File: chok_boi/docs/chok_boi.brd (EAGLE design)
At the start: 160 x 100 mm, 94 parts, among them IC1 L293DD, U1 MPU-6000

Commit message: Place all big components on board
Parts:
- removed U$10: EMITTER, sfh4550 _ teft4300:EMITTER
- removed U$6: RECEIVER, sfh4550 _ teft4300:RECEIVER
- added LEFT_FRONT_EMITTER: EMITTER, sfh4550 _ teft4300:EMITTER
- added REC_LF: RECEIVER, sfh4550 _ teft4300:RECEIVER
- moved T1 370.0 mm to (16.0, 13.5)
- moved T3 352.3 mm to (17.0, 59.2)
- moved L1 350.4 mm to (16.3, 19.8)
- moved B1 349.5 mm to (5.59, 4.06)
- moved U$20 348.2 mm to (65.8, 10.4), turned to 180 degrees
- moved T2 344.8 mm to (13.5, 59.7)
- moved SERIAL2 344.5 mm to (56.9, 52.3)
- moved U1 343.9 mm to (69.1, 36.8)
- moved C_BAT2 342.3 mm to (13.2, 48.3)
- moved C_5V2 340.4 mm to (13.2, 44.7)
- moved B0 339.5 mm to (5.59, 10.7)
- moved U$8 336.4 mm to (73.9, 20.1), turned to 218.7 degrees
- moved U$9 336.3 mm to (77.5, 32.8), turned to 270 degrees
- moved SERIAL1 332.1 mm to (56.6, 57.4)
- moved LED_PWR 332.0 mm to (13.2, 51.8)
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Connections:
- net N$14 renamed H_EM
- net N$15 renamed H2_EM
- net N$17 renamed D2_EM
- net N$27 renamed RF_EM
- net N$9 renamed D_EM
- removed net N$5: R_ELF.2, U$10.-
- new net LF_EM: LEFT_FRONT_EMITTER.-, R_ELF.2
- net 5V: now also LEFT_FRONT_EMITTER.+; no longer U$10.+
- net A3.3V: now also REC_LF.C; no longer U$6.C
- net REC_LF: now also REC_LF.E; no longer U$6.E

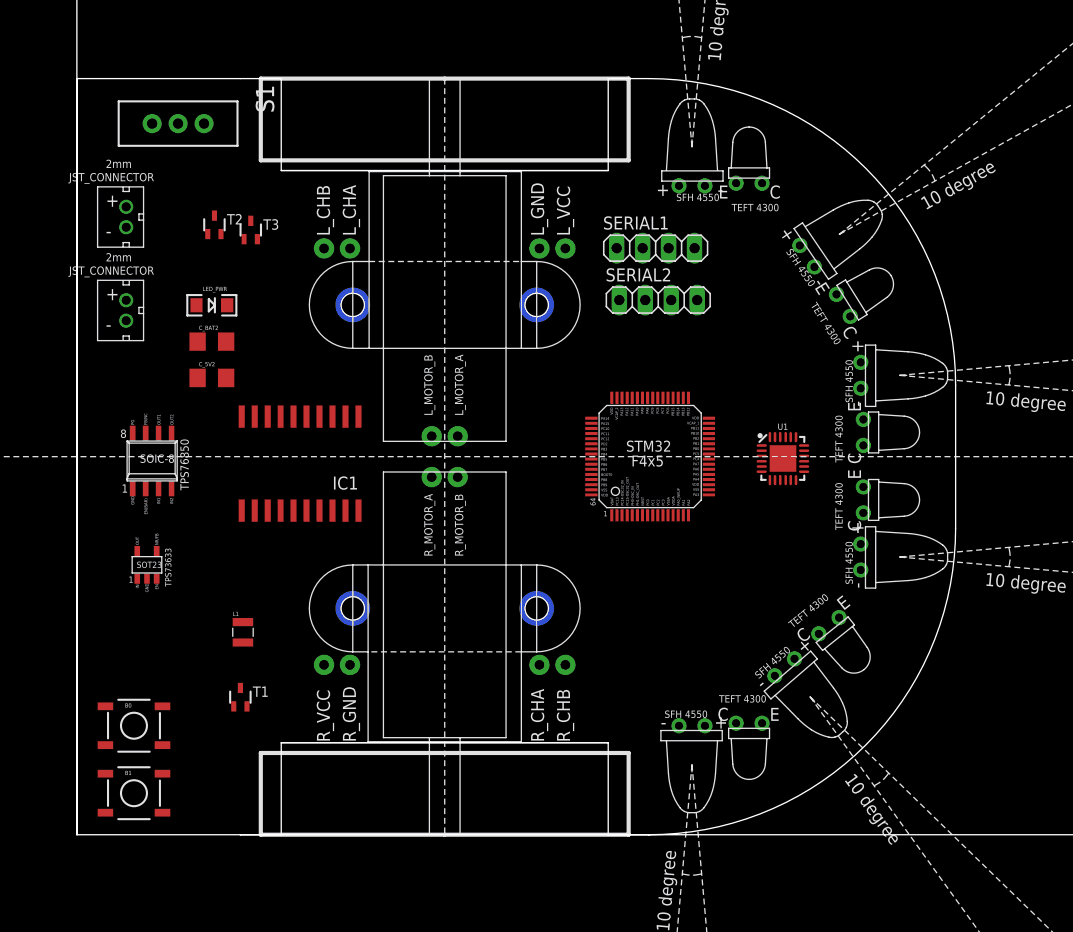
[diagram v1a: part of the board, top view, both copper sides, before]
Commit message: Add power and gnd planes
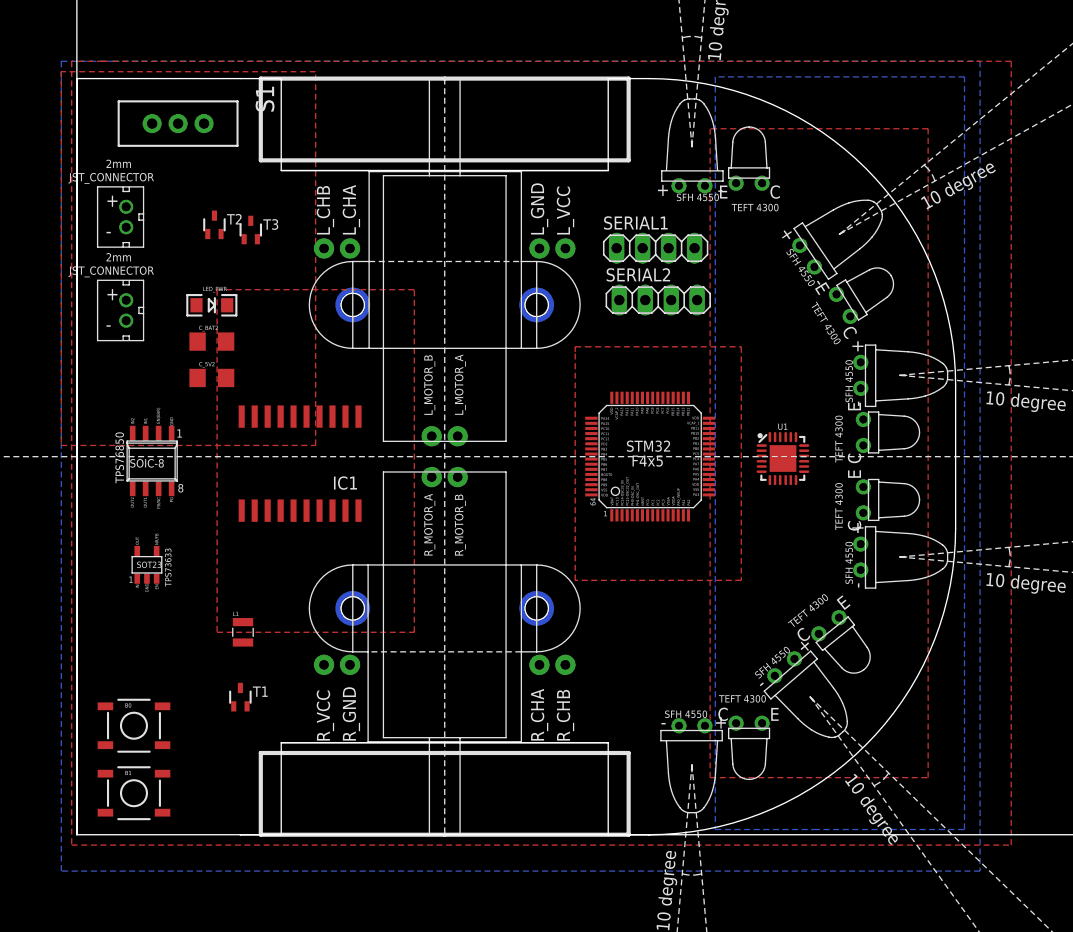
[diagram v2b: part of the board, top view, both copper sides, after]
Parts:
- turned U$4 to 180 degrees
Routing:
- added copper zone on layer 1, net 3.3V
- added copper zone on layer 1, net 5V
- added copper zone on layer 1, net A3.3V
- added copper zone on layer 16, net AGND
- added copper zone on layer 1, net BATTERY
- added copper zone on layer 16, net GND
- added copper zone on layer 1, net MGND

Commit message: Change part names for easier routing
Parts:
- removed C_5V4, C_5V5, C_5V6, C_5V7, C_5V8, C_5V9: 0.1uF, SparkFun:0603-CAP
- removed C_ERF3, C_S2: 0.1uF, SparkFun-Capacitors:0603-CAP
- removed C_ERF4, C_S1: 4.7uF, SparkFun-Capacitors:0603-CAP
- removed R_ES1, R_ES2, R_ES3, R_ES4: 5.6, SparkFun-Passives:0603-RES
- removed R_RLS, R_RRF1, R_RRF2, R_RRS: 1.8k, SparkFun-Passives:0603-RES
- added C_EM_D1, C_E_H1: 4.7uF, SparkFun-Capacitors:0603-CAP
- added C_EM_D2, C_E_H2: 0.1uF, SparkFun-Capacitors:0603-CAP
- added C_REC_LD, C_REC_LF, C_REC_LH, C_REC_RD, C_REC_RF, C_REC_RH: 0.1uF, SparkFun:0603-CAP
- added R_ED1, R_ED2, R_EH1, R_EH2: 5.6, SparkFun-Passives:0603-RES
- added R_RLD, R_RLH, R_RRD, R_RRH: 1.8k, SparkFun-Passives:0603-RES
- moved R_RRF 436.6 mm to (73.7, 25.7)
- moved R_RLF 417.1 mm to (73.2, 44.5)
- moved U$16 408.5 mm to (20.6, 44.5)
- moved U$15 405.7 mm to (20.6, 46.0)
- moved C_3.3V1 356.8 mm to (196.6, 92.7)
- moved C_3.3V2 356.8 mm to (192.8, 92.7)
- moved C_5V1 356.8 mm to (189.0, 92.7)
- moved C_5V10 356.8 mm to (162.3, 92.7)
- moved C_5V11 356.8 mm to (158.5, 92.7)
- moved C_5V12 356.8 mm to (154.7, 92.7)
- moved C_BAT1 356.8 mm to (150.9, 92.7)
- moved C_ELF1 356.8 mm to (147.1, 92.7)
- moved C_ELF2 356.8 mm to (143.3, 92.7)
- moved C_ERF1 356.8 mm to (139.4, 92.7)
- moved C_ERF2 356.8 mm to (135.6, 92.7)
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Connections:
- net 5V: now also C_EM_D1.1, C_EM_D2.1, C_E_H1.1, C_E_H2.1; no longer C_ERF3.1, C_ERF4.1, C_S1.1, C_S2.1
- net A3.3V: now also C_REC_LD.1, C_REC_LF.1, C_REC_LH.1, C_REC_RD.1, C_REC_RF.1, C_REC_RH.1; no longer C_5V4.1, C_5V5.1, C_5V6.1, C_5V7.1, C_5V8.1, C_5V9.1
- net AGND: now also C_REC_LD.2, C_REC_LF.2, C_REC_LH.2, C_REC_RD.2, C_REC_RF.2, C_REC_RH.2, R_RLD.1, R_RLH.1, R_RRD.1, R_RRH.1; no longer C_5V4.2, C_5V5.2, C_5V6.2, C_5V7.2, C_5V8.2, C_5V9.2, R_RLS.1, R_RRF1.1, R_RRF2.1, R_RRS.1
- net D2_EM: now also R_ED1.2, R_ED2.2; no longer R_ES1.2, R_ES2.2
- net GND: now also C_EM_D1.2, C_EM_D2.2, C_E_H1.2, C_E_H2.2; no longer C_ERF3.2, C_ERF4.2, C_S1.2, C_S2.2
- net H2_EM: now also R_EH1.2, R_EH2.2; no longer R_ES3.2, R_ES4.2
- net N$18: now also R_ED1.1, R_ED2.1; no longer R_ES1.1, R_ES2.1
- net N$19: now also R_EH1.1, R_EH2.1; no longer R_ES3.1, R_ES4.1
- net REC_LD: now also R_RLD.2; no longer R_RLS.2
- net REC_LH: now also R_RLH.2; no longer R_RRF2.2
- net REC_RD: now also R_RRD.2; no longer R_RRS.2
- net REC_RH: now also R_RRH.2; no longer R_RRF1.2

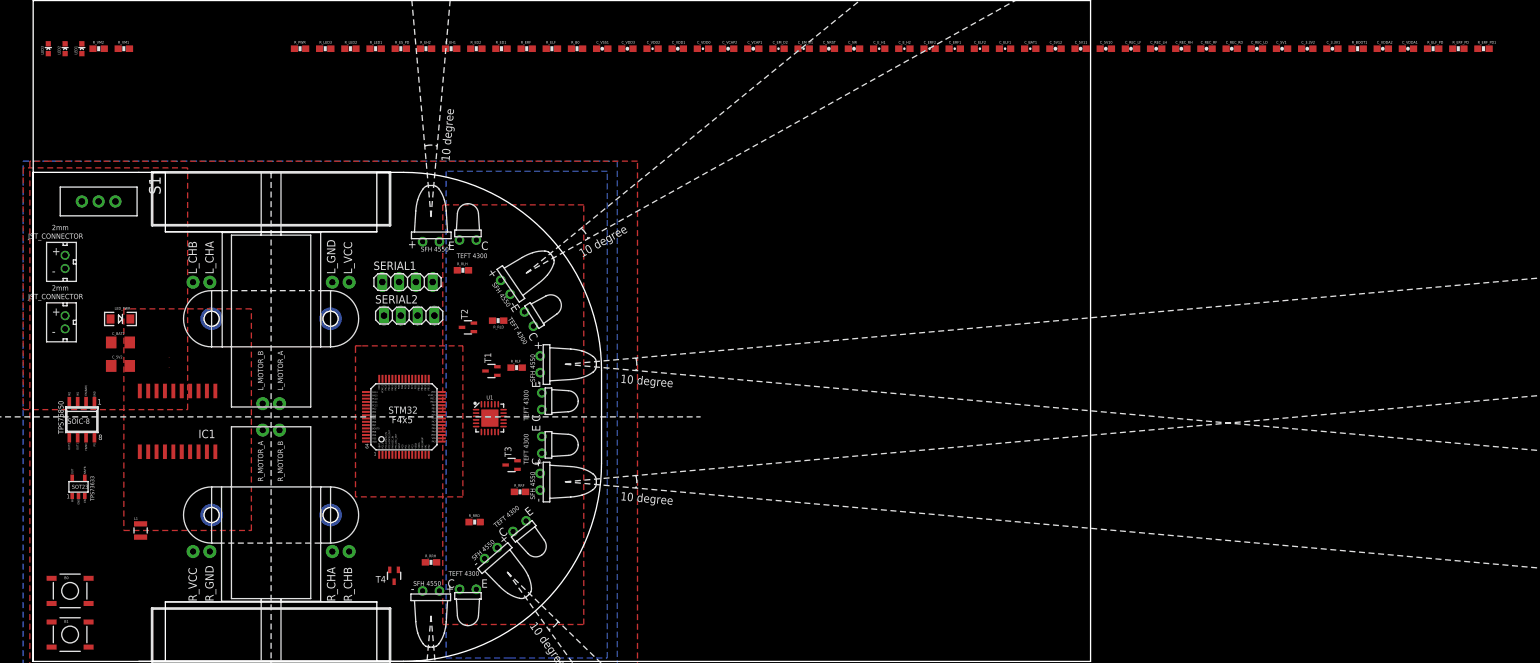
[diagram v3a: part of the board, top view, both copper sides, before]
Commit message: Finish component placement. Start routing
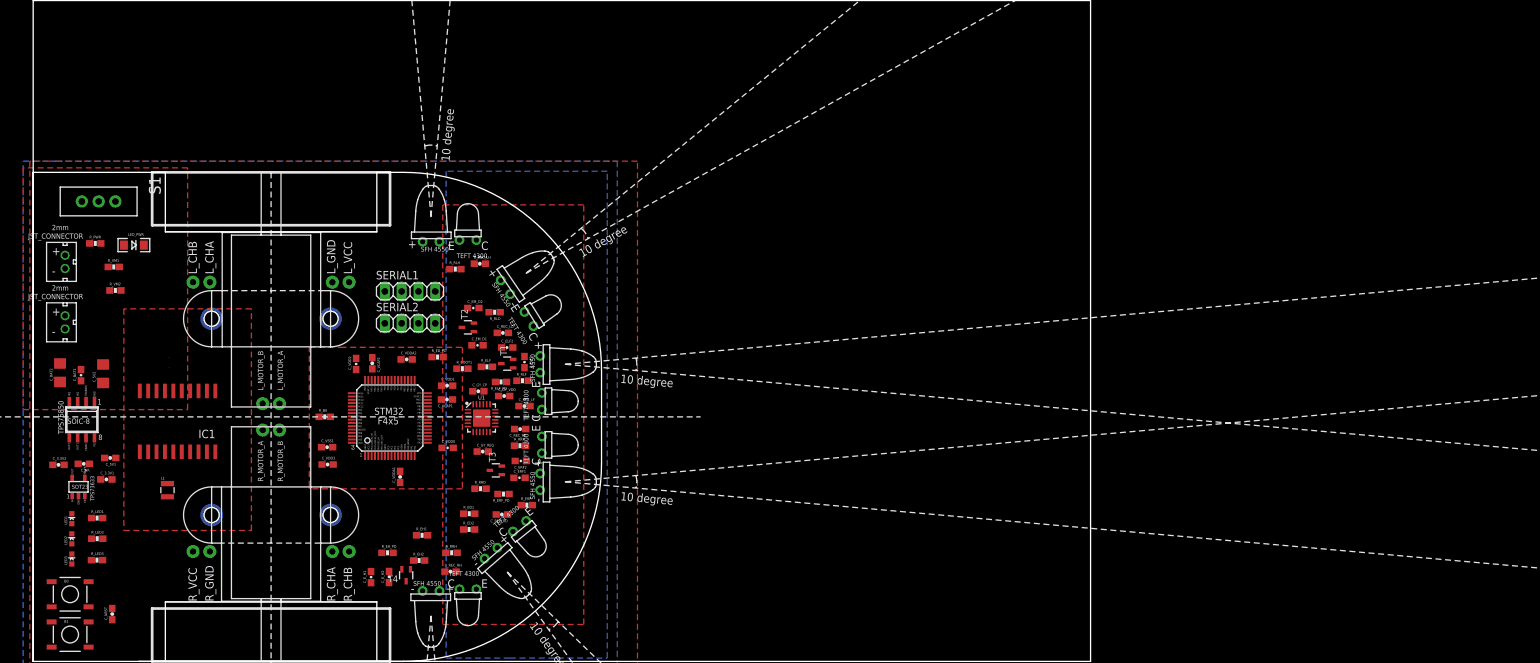
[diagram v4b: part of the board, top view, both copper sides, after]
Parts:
- removed C_5V10: 0.01uF, SparkFun:0603-CAP
- removed C_5V11: 0.1uF, SparkFun:0603-CAP
- removed C_5V12: 2.2nF, SparkFun:0603-CAP
- removed R_ERF_PD1, R_ES_PD: 47k, SparkFun-Passives:0603-RES
- added C_GY_CP: 2.2nF, SparkFun:0603-CAP
- added C_GY_REG: 0.1uF, SparkFun:0603-CAP
- added C_GY_VDD: 0.01uF, SparkFun:0603-CAP
- added R_ED_PD, R_EH_PD: 47k, SparkFun-Passives:0603-RES
- moved C_3.3V2 199.2 mm to (3.84, 29.7)
- moved C_3.3V1 196.6 mm to (11.1, 27.5)
- moved C_5V1 187.8 mm to (11.7, 30.8), turned to 180 degrees
- moved C_VDDA1 165.7 mm to (55.5, 27.9), turned to 90 degrees
- moved R_ERF_PD 159.4 mm to (71.2, 25.3), turned to 180 degrees
- moved C_VDDA2 155.0 mm to (56.5, 45.7)
- moved C_BAT1 151.9 mm to (7.24, 43.3), turned to 90 degrees
- moved R_ELF_PD 149.8 mm to (70.8, 42.3), turned to 180 degrees
- moved R_BOOT1 143.8 mm to (64.9, 44.3)
- moved C_NRST 138.1 mm to (12.0, 7.16), turned to 90 degrees
- moved C_REC_RH 136.0 mm to (63.1, 13.6)
- moved C_NR 132.4 mm to (7.65, 29.9), turned to 180 degrees
- moved C_REC_RD 131.0 mm to (70.9, 22.2), turned to 180 degrees
- moved C_REC_LD 121.9 mm to (71.1, 49.7)
- moved C_REC_RF 118.7 mm to (73.7, 35.2), turned to 180 degrees
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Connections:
- net A3.3V: now also C_GY_VDD.1; no longer C_5V10.1
- net AGND: now also C_GY_CP.2, C_GY_REG.2, C_GY_VDD.2; no longer C_5V10.2, C_5V11.2, C_5V12.2
- net EM_D: now also R_ED_PD.2; no longer R_ES_PD.2
- net EM_H: now also R_EH_PD.2; no longer R_ERF_PD1.2
- net GND: now also R_ED_PD.1, R_EH_PD.1; no longer R_ERF_PD1.1, R_ES_PD.1
- net N$20: now also C_GY_REG.1; no longer C_5V11.1
- net N$22: now also C_GY_CP.1; no longer C_5V12.1

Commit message: 117 Airwires Left
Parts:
- moved C_VDDA2 17.6 mm to (57.5, 28.2), turned to 270 degrees
- moved L1 9.15 mm to (11.3, 24.5), turned to 90 degrees
- moved R_VM1 5.97 mm to (16.3, 55.3)
- moved R_VM2 3.09 mm to (14.3, 58.6)
- moved C_VDD3 1.15 mm to (44.5, 30.9)
- moved R_LED3 1.13 mm to (9.07, 16.3), turned to 180 degrees
- moved C_VSS1 0.94 mm to (44.6, 33.4)
- moved R_LED1 0.77 mm to (8.92, 21.6), turned to 180 degrees
- moved R_LED2 0.76 mm to (9.03, 18.9), turned to 180 degrees
- moved C_VDDA1 0.60 mm to (55.0, 28.2)
- moved C_ERF1 0.31 mm to (73.8, 28.0), turned to 180 degrees
- moved B0 0.14 mm to (5.64, 10.0)
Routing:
- net GND: track 0.00 -> 203.2 mm, vias 0 -> 3
- net 5V: track 0.00 -> 87.1 mm, vias 0 -> 4
- net BATTERY: track 0.00 -> 26.2 mm, vias 0 -> 2
- net 3.3V: track 0.00 -> 23.9 mm
- net AGND: track 0.00 -> 11.1 mm
- net N$8: track 0.00 -> 10.7 mm
- net H2_EM: track 0.00 -> 9.44 mm
- net N$2: track 0.00 -> 9.20 mm
- net N$19: track 0.00 -> 8.82 mm
- net D2_EM: track 0.00 -> 7.43 mm
- net N$1: track 0.00 -> 7.14 mm
- net REC_RH: track 0.00 -> 6.92 mm
- net A3.3V: track 0.00 -> 5.77 mm
- net VOLTMETER: track 0.00 -> 4.40 mm
- net BOOT0: track 0.00 -> 4.40 mm
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- removed copper zone on layer 1, net A3.3V

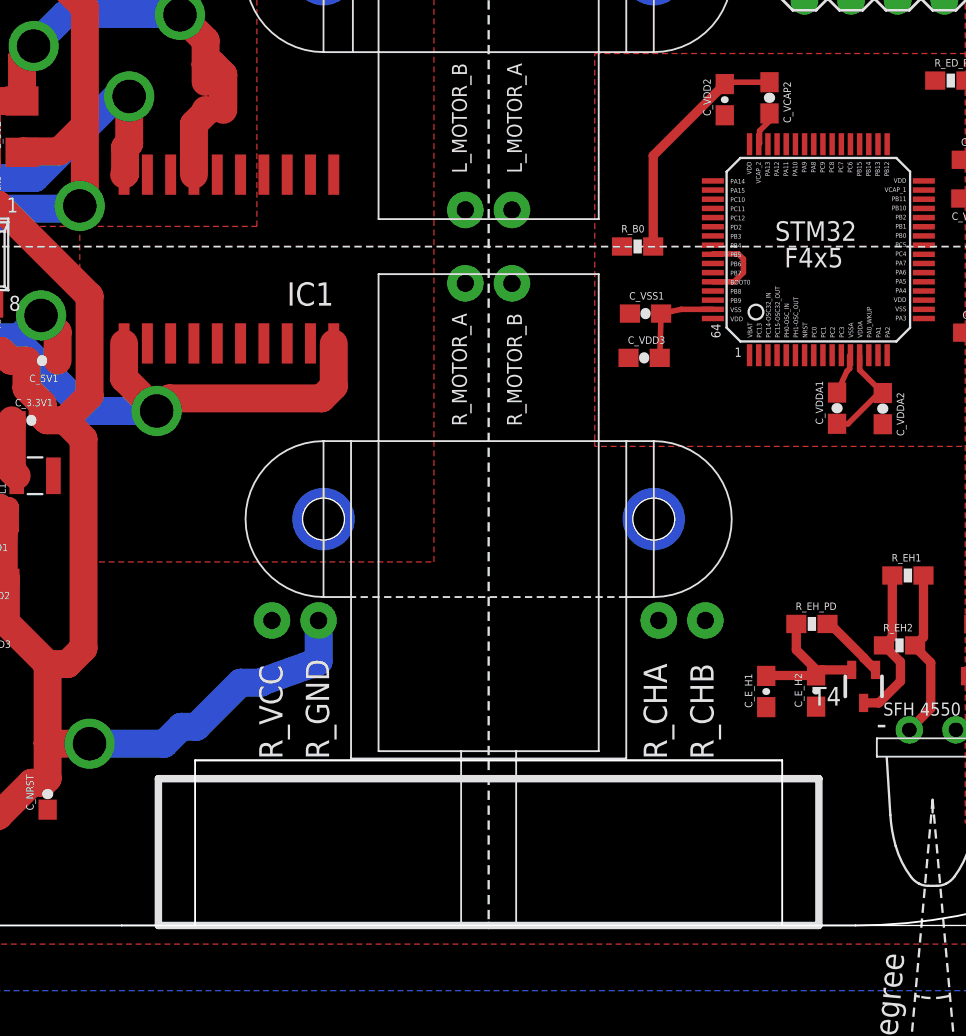
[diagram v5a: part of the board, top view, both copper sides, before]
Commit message: Add DRV8835 motor driver
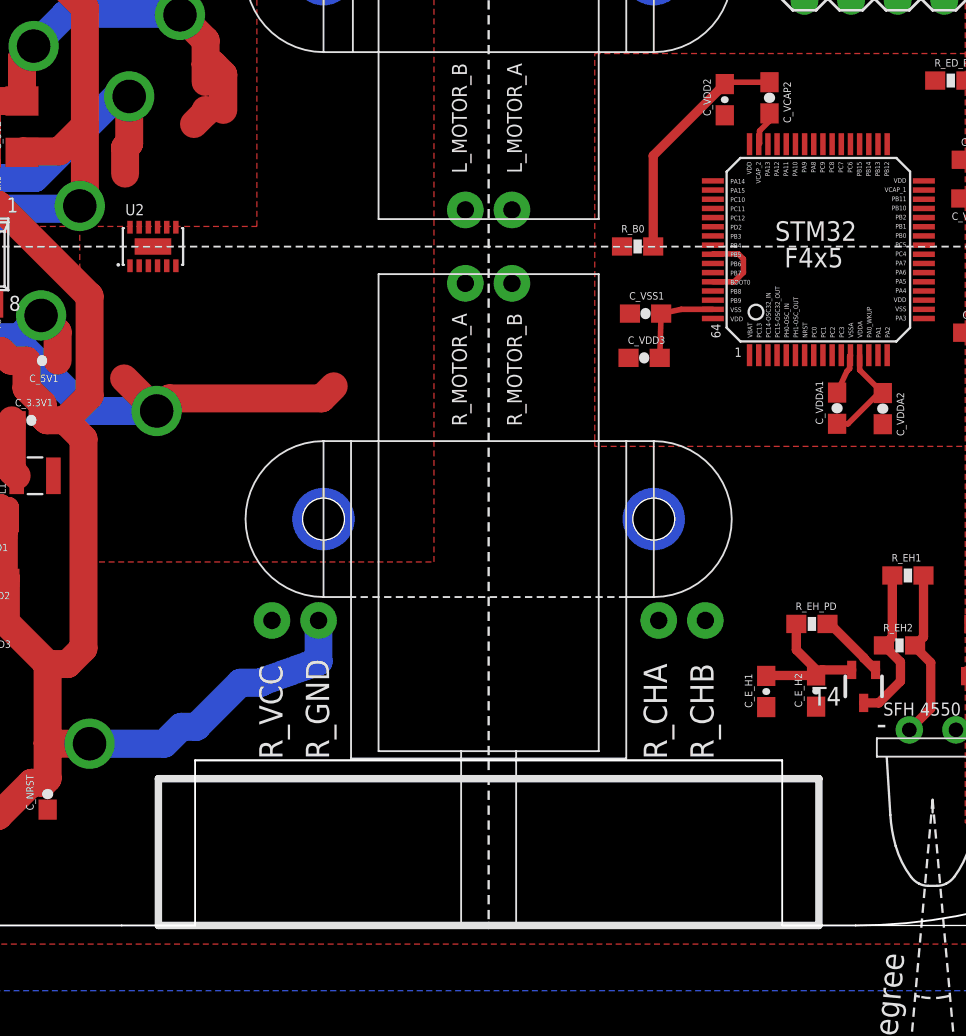
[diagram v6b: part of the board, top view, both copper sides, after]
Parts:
- removed IC1: L293DD, st-microelectronics:SO20
- added U2: DRV8835, SparkFun-IC-Special-Function:WSON-12
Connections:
- new net MODE: U2.11
- net 3.3V: now also U2.12
- net 5V: no longer IC1.1, IC1.11, IC1.20
- net BATTERY: now also U2.1; no longer IC1.10
- net MGND: now also U2.6, U2.PAD; no longer IC1.14, IC1.15, IC1.16, IC1.17, IC1.4, IC1.5, IC1.6, IC1.7
- net MLB: now also U2.2; no longer IC1.3
- net MLF: now also U2.3; no longer IC1.8
- net MRB: now also U2.4; no longer IC1.13
- net MRF: now also U2.5; no longer IC1.18
- net PWMLB: now also U2.10; no longer IC1.2
- net PWMLF: now also U2.9; no longer IC1.9
- net PWMRB: now also U2.8; no longer IC1.12
- net PWMRF: now also U2.7; no longer IC1.19
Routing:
- net 5V: track 87.1 -> 82.8 mm
- net MGND: track 3.79 -> 1.03 mm
